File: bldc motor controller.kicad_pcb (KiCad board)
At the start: 4 copper layers, 26 x 26 mm, 50 parts, among them J1 Conn_01x04_Pin, M2 MountingHole_2.2mm_M2_DIN965_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, U1 C47023655, U3 C529358, U6 C126671

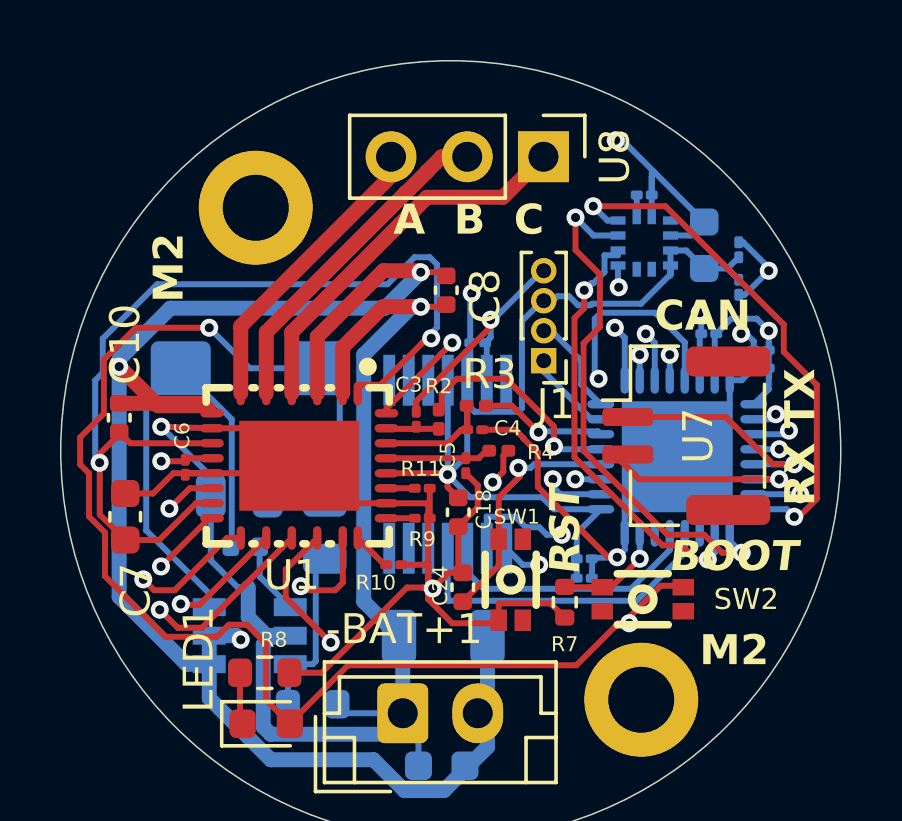
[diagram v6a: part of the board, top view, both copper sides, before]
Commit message: updated certain capacitor sizes, doubled power vias for saftey
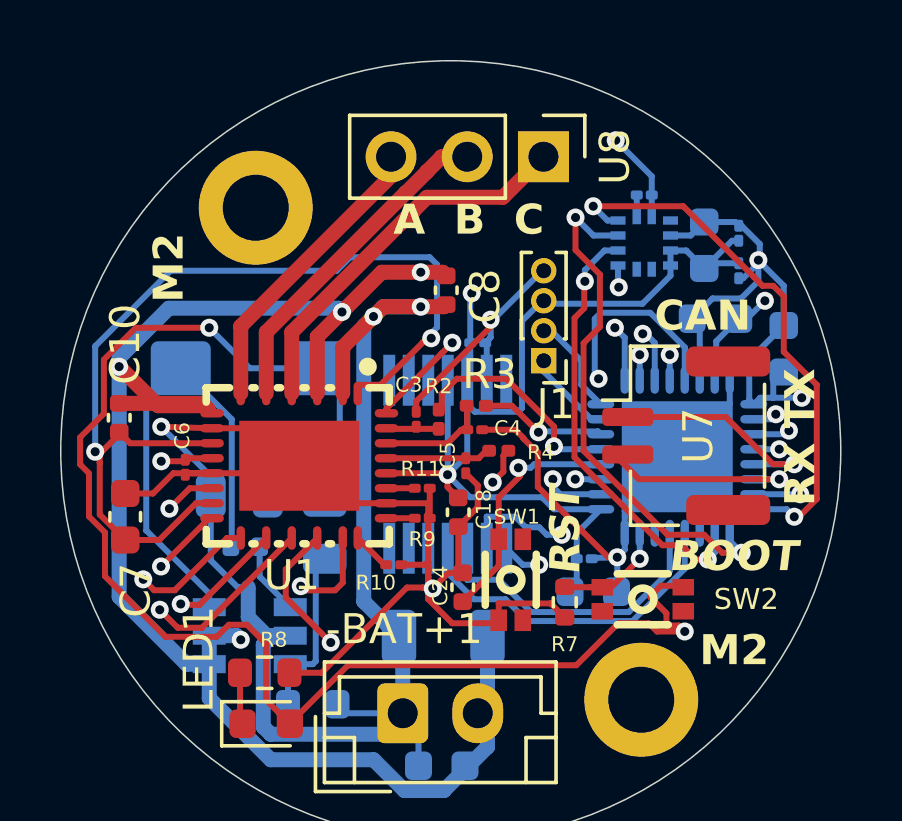
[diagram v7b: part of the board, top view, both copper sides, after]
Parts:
- C13, C15, C17: footprint Capacitor_SMD:C_01005_0402Metric -> Capacitor_SMD:C_0603_1608Metric
- moved C15 0.75 mm to (153.6, 84.6), turned to -90 degrees
- moved C21 0.55 mm to (152.1, 82.0)
- moved C23 0.55 mm to (152.1, 80.8)
- moved C13 0.55 mm to (151.3, 83.6)
- moved C17 0.54 mm to (147.2, 92.7)
- moved C14 0.47 mm to (152.4, 85.0), turned to -90 degrees
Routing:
- net +BATT: track 77.4 -> 85.4 mm, vias 3 -> 4
- net TI_AGND: track 77.4 -> 81.7 mm, vias 8 -> 6
- net TI_VREF: track 136.1 -> 139.8 mm, vias 5 -> 6
- net MISO1: track 8.87 -> 10.1 mm
- net -BATT: track 48.4 -> 49.1 mm, vias 1 -> 2
- net SDA1: track 17.7 -> 18.3 mm

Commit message: Big push before imu swap
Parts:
- moved SW1 0.11 mm to (144.6, 92.2)
- moved SW2 0.07 mm to (148.9, 92.9)
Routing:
- net TI_VREF: track 139.8 -> 138.6 mm
- net ENAB_XL: track 14.6 -> 15.7 mm
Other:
- board text added: "- +"
- board text added: "ON"
